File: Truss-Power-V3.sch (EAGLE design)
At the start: 31 parts, among them J1 XF2L-0535-1, U1 TPS61090, U2 MCP73831T-2ACI/OT, U3 MAX17044, X1 22-23-2021, X2 MicroB, X3 22-23-2021, X4 CON-1PIN

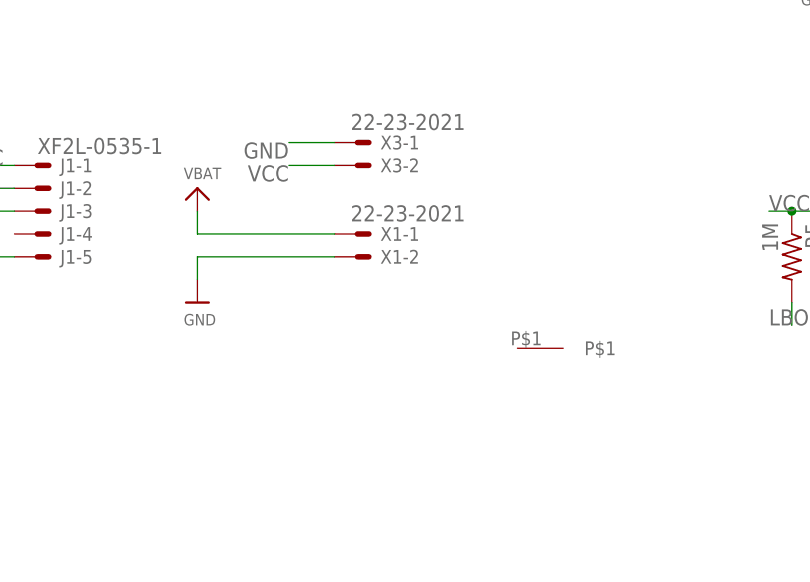
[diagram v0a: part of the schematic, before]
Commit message: v3 truss power battery connector updated
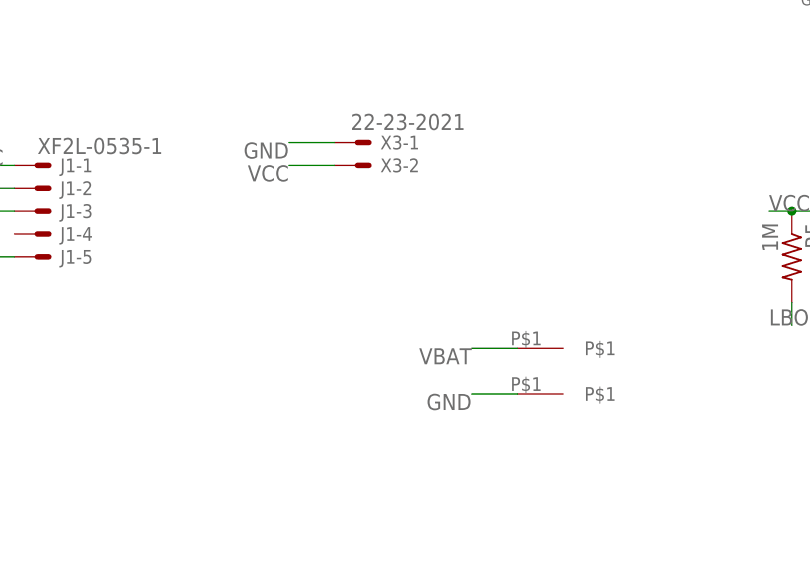
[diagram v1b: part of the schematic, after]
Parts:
- removed X1: 22-23-2021, con-molex:22-23-2021
- added X5: CON-1PIN, NewPart:CON-1PIN
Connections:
- net GND: now also X5.P$1; no longer X1-2.S
- net VBAT: now also X4.P$1; no longer X1-1.S
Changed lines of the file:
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@@
 <?xml version="1.0" encoding="utf-8"?>
 <!DOCTYPE eagle SYSTEM "eagle.dtd">
-<eagle version="8.3.2">
+<eagle version="8.4.3">
 <drawing>
 <settings>
@@
 <part name="C3" library="microbuilder" deviceset="CAP_CERAMIC" device="0805-NOOUTLINE" value="10µF"/>
 <part name="U$15" library="microbuilder" deviceset="GND" device=""/>
-<part name="X1" library="con-molex" library_urn="urn:adsk.eagle:library:165" deviceset="22-23-2021" device=""/>
-<part name="U$16" library="microbuilder" deviceset="VBAT" device=""/>
-<part name="U$17" library="microbuilder" deviceset="GND" device=""/>
 <part name="U3" library="NewPart" deviceset="MAX17044" device=""/>
 <part name="R6" library="resistor" deviceset="R-US_" device="R0402" value="1K"/>
@@
 <part name="R7" library="resistor" deviceset="R-US_" device="R0402" value="470"/>
 <part name="X4" library="NewPart" deviceset="CON-1PIN" device=""/>
+<part name="X5" library="NewPart" deviceset="CON-1PIN" device=""/>
 </parts>
 <sheets>
@@
 <instance part="C3" gate="G$1" x="119.38" y="76.2"/>
 <instance part="U$15" gate="G$1" x="119.38" y="68.58"/>
-<instance part="X1" gate="-1" x="99.06" y="15.24"/>
-<instance part="X1" gate="-2" x="99.06" y="12.7"/>
-<instance part="U$16" gate="G$1" x="81.28" y="20.32"/>
-<instance part="U$17" gate="G$1" x="81.28" y="7.62"/>
 <instance part="U3" gate="G$1" x="175.26" y="63.5"/>
 <instance part="R6" gate="G$1" x="142.24" y="68.58"/>
@@
 <instance part="R7" gate="G$1" x="60.96" y="76.2" rot="R180"/>
 <instance part="X4" gate="G$1" x="121.92" y="2.54"/>
+<instance part="X5" gate="G$1" x="121.92" y="-2.54"/>
 </instances>
 <busses>
@@
 </segment>
 <segment>
-<pinref part="X1" gate="-2" pin="S"/>
-<pinref part="U$17" gate="G$1" pin="GND"/>
-<wire x1="96.52" y1="12.7" x2="81.28" y2="12.7" width="0.1524" layer="91"/>
-<wire x1="81.28" y1="12.7" x2="81.28" y2="10.16" width="0.1524" layer="91"/>
-</segment>
-<segment>
 <wire x1="157.48" y1="53.34" x2="157.48" y2="45.72" width="0.1524" layer="91"/>
 <pinref part="U3" gate="G$1" pin="GND"/>
@@
 <wire x1="48.26" y1="43.18" x2="55.88" y2="43.18" width="0.1524" layer="91"/>
 <wire x1="55.88" y1="43.18" x2="55.88" y2="40.64" width="0.1524" layer="91"/>
+</segment>
+<segment>
+<pinref part="X5" gate="G$1" pin="P$1"/>
+<wire x1="116.84" y1="-2.54" x2="111.76" y2="-2.54" width="0.1524" layer="91"/>
+<label x="111.76" y="-2.54" size="1.778" layer="95" rot="R180"/>
 </segment>
 </net>
@@
 </segment>
 <segment>
-<pinref part="U$16" gate="G$1" pin="VBAT"/>
-<pinref part="X1" gate="-1" pin="S"/>
-<wire x1="81.28" y1="17.78" x2="81.28" y2="15.24" width="0.1524" layer="91"/>
-<wire x1="81.28" y1="15.24" x2="96.52" y2="15.24" width="0.1524" layer="91"/>
-</segment>
-<segment>
 <pinref part="U$8" gate="G$1" pin="VBAT"/>
 <pinref part="R11" gate="G$1" pin="1"/>
@@
 <label x="50.8" y="20.32" size="1.778" layer="95"/>
 </segment>
+<segment>
+<pinref part="X4" gate="G$1" pin="P$1"/>
+<wire x1="116.84" y1="2.54" x2="111.76" y2="2.54" width="0.1524" layer="91"/>
+<label x="111.76" y="2.54" size="1.778" layer="95" rot="R180"/>
+</segment>
 </net>

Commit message: 6-Pin FPC updated.
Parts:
- added D1: (no value), diode:DIODE-SOD523
- added IC1: 74AUC1G06DCK, 74xx-little-us:74AUC1G06DCK
- J1: value XF2L-0535-1 -> XF2L-0625-1; device con-omron:XF2L-0535-1 -> con-omron:XF2L-0625-1
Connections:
- removed net EN_SIG: J1-5.MS
- removed net EN_SW: J1-3.MS
- new net DETSW_P: J1-4.MS
- new net PWRSW_P: D1.A, J1-3.MS
- net LEDSOC: now also J1-1.MS; no longer J1-1.MSV
- net SCL: now also J1-6.MS
- net SDA: now also J1-5.MS
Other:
- note added: "BOOST"
- note added: "CHARGER"
- note added: "CONNECTOR"
- note added: "GAUGE"

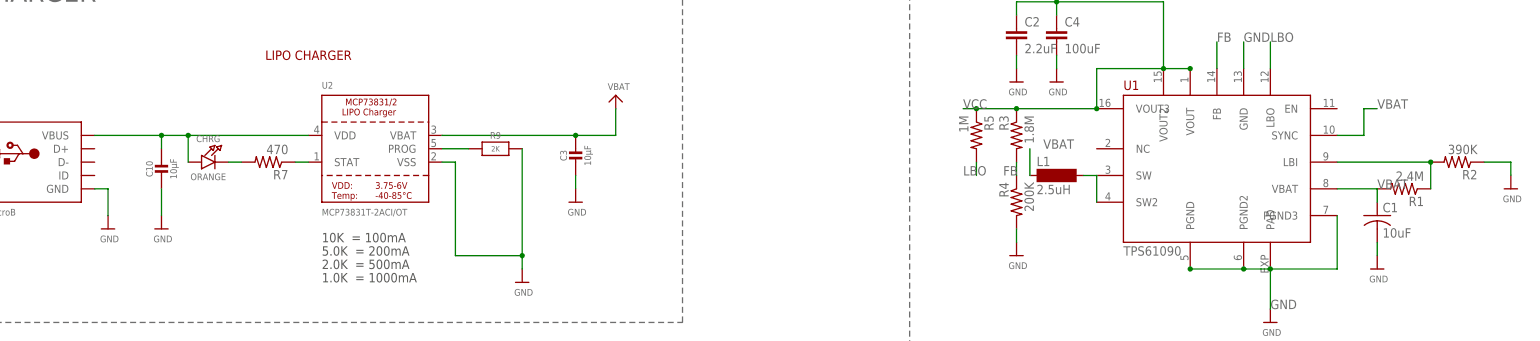
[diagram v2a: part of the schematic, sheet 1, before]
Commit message: Charger circuitry updated; Inverter and diode-or added for Boost EN
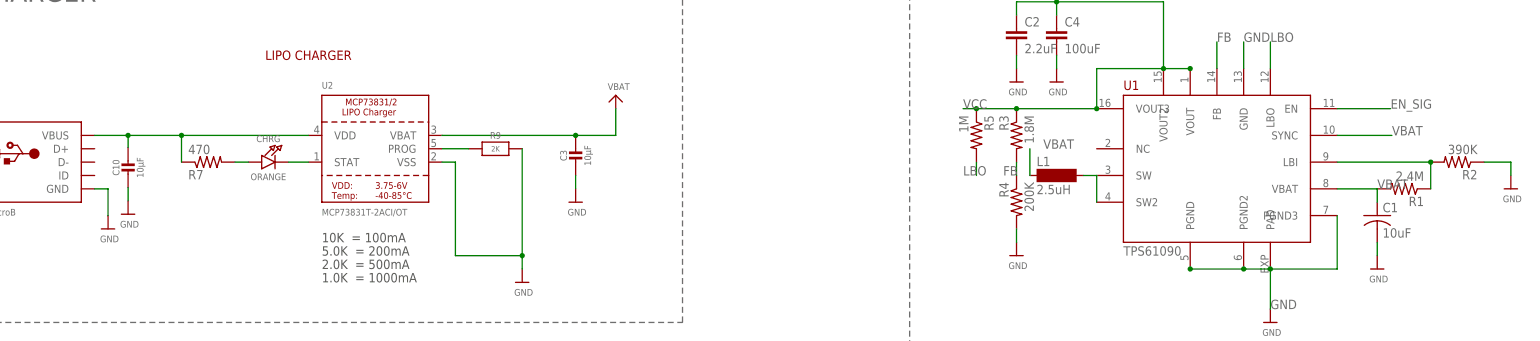
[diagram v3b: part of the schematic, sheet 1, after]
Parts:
- removed IC1: 74AUC1G06DCK, 74xx-little-us:74AUC1G06DCK
- added D2: (no value), diode:DIODE-SOD523
- added U$16: INVERTER-GATE, NewPart:INVERTER-GATE
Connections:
- removed net N$12: CHRG.C, R7.2
- removed net N$13: R7.1, U2.STAT
- new net EN_SIG: D1.C, D2.C, U1.EN
- new net N$5: D2.A, U$16.P$2
- new net N$6: CHRG.A, R7.2
- new net N$7: CHRG.C, U2.STAT
- net DETSW_P: now also U$16.P$1
- net GND: now also U$16.GND
- net VBAT: now also U$16.VBAT
- net VBUS: now also R7.1; no longer CHRG.A
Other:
- moved on the sheet: C10, CHRG, R7

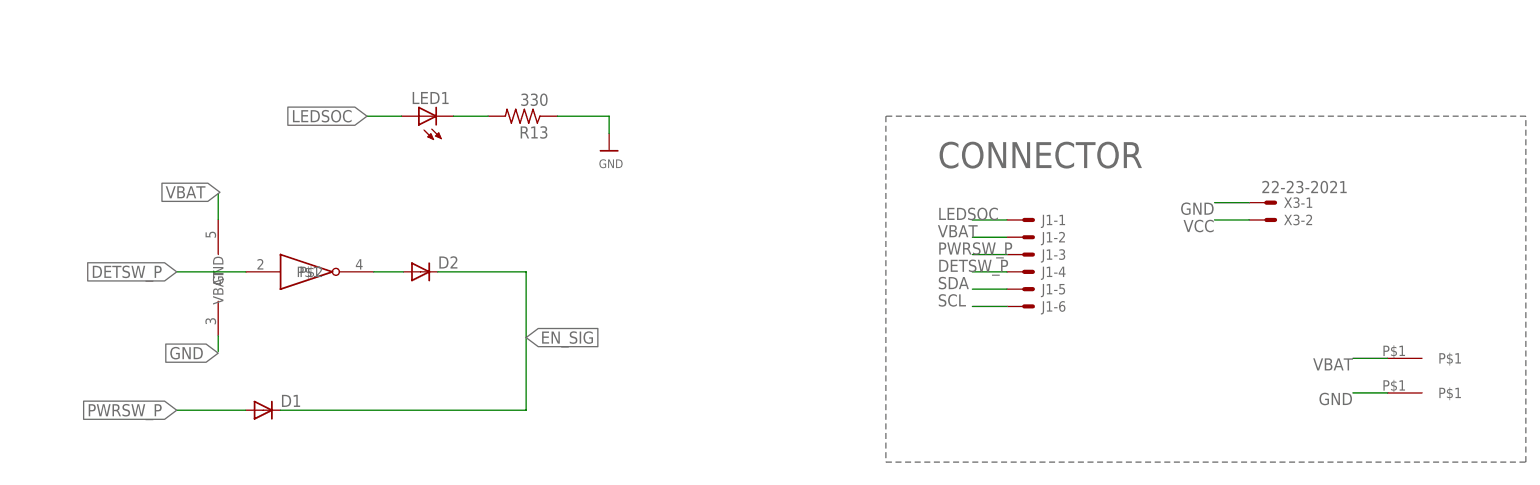
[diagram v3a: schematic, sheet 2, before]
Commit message: XOR Gate added in library; XOR gate added for Boost EN
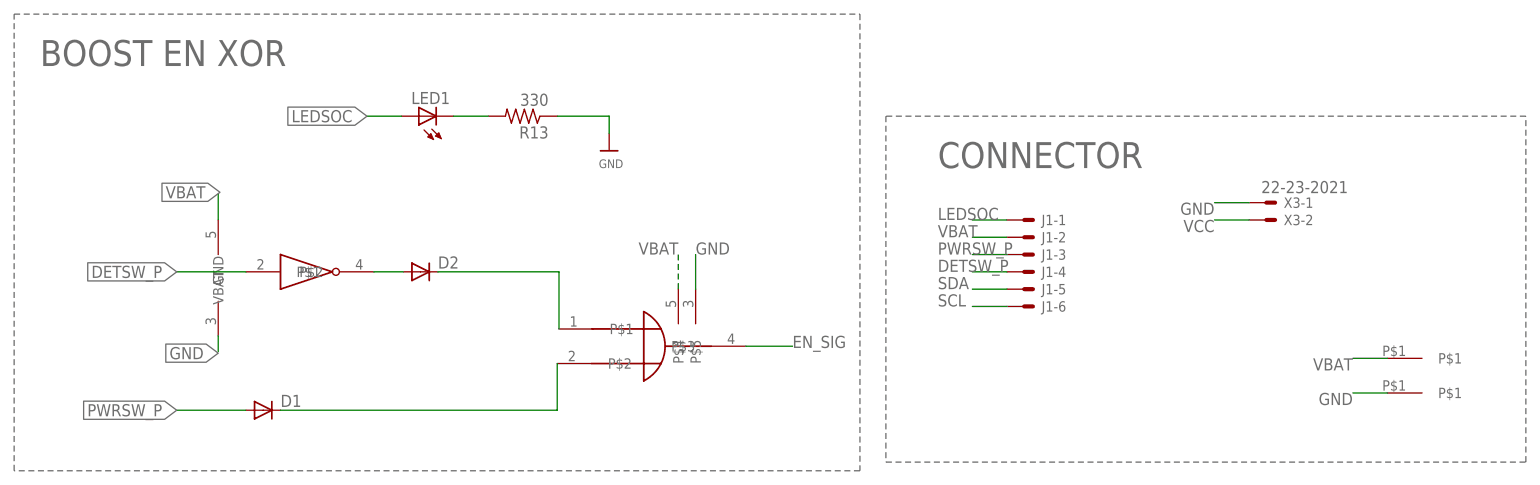
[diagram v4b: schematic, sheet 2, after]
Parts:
- added U4: SN74LVC1G86DC1LR, NewPart:SN74LVC1G86DC1LR
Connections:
- new net DETSW_D: D2.C, U4.P$1
- new net PWRSW_D: D1.C, U4.P$2
- net EN_SIG: now also U4.P$3; no longer D1.C, D2.C
- net GND: now also U4.P$5
- net VBAT: now also U4.P$4
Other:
- note added: "BOOST EN XOR"
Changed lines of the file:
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@@
 <part name="U$16" library="NewPart" deviceset="INVERTER-GATE" device=""/>
 <part name="D2" library="diode" library_urn="urn:adsk.eagle:library:210" deviceset="DIODE-" device="SOD523" package3d_urn="urn:adsk.eagle:package:43410/1"/>
+<part name="U4" library="NewPart" deviceset="SN74LVC1G86DC1LR" device=""/>
 </parts>
 <sheets>
@@
 <wire x1="200.66" y1="76.2" x2="106.68" y2="76.2" width="0.1524" layer="95" style="longdash"/>
 <text x="114.3" y="68.58" size="3.81" layer="95">CONNECTOR</text>
+<wire x1="-21.336" y1="91.186" x2="102.87" y2="91.186" width="0.1524" layer="95" style="longdash"/>
+<wire x1="102.87" y1="91.186" x2="102.87" y2="24.13" width="0.1524" layer="95" style="longdash"/>
+<wire x1="102.87" y1="24.13" x2="-21.336" y2="24.13" width="0.1524" layer="95" style="longdash"/>
+<wire x1="-21.336" y1="24.13" x2="-21.336" y2="91.186" width="0.1524" layer="95" style="longdash"/>
+<text x="-17.526" y="83.566" size="3.81" layer="95">BOOST EN XOR</text>
 </plain>
 <instances>
@@
 <instance part="U$16" gate="G$1" x="20.32" y="53.34"/>
 <instance part="D2" gate="G$1" x="38.354" y="53.34"/>
+<instance part="U4" gate="G$1" x="71.12" y="42.418"/>
 </instances>
 <busses>
@@
 <label x="8.636" y="41.402" size="1.778" layer="95" rot="R180" xref="yes"/>
 </segment>
+<segment>
+<wire x1="78.74" y1="55.88" x2="78.74" y2="50.8" width="0.1524" layer="91"/>
+<pinref part="U4" gate="G$1" pin="P$5"/>
+<label x="78.74" y="55.88" size="1.778" layer="95"/>
+</segment>
 </net>
 <net name="VBAT" class="0">
@@
 <label x="8.89" y="65.024" size="1.778" layer="95" rot="R180" xref="yes"/>
 </segment>
+<segment>
+<pinref part="U4" gate="G$1" pin="P$4"/>
+<wire x1="76.2" y1="50.8" x2="76.2" y2="55.88" width="0.1524" layer="91" style="longdash"/>
+<label x="76.2" y="57.658" size="1.778" layer="95" rot="R180"/>
+</segment>
 </net>
 <net name="VCC" class="0">
@@
 </segment>
 </net>
+<net name="DETSW_D" class="0">
+<segment>
+<pinref part="D2" gate="G$1" pin="C"/>
+<wire x1="40.894" y1="53.34" x2="58.674" y2="53.34" width="0.1524" layer="91"/>
+<pinref part="U4" gate="G$1" pin="P$1"/>
+<wire x1="58.674" y1="44.958" x2="58.674" y2="53.34" width="0.1524" layer="91"/>
+</segment>
+</net>
+<net name="PWRSW_D" class="0">
+<segment>
+<pinref part="D1" gate="G$1" pin="C"/>
+<wire x1="17.78" y1="33.02" x2="58.42" y2="33.02" width="0.1524" layer="91"/>
+<pinref part="U4" gate="G$1" pin="P$2"/>
+<wire x1="58.42" y1="39.878" x2="58.42" y2="33.02" width="0.1524" layer="91"/>
+</segment>
+</net>
 <net name="EN_SIG" class="0">
 <segment>
-<pinref part="D1" gate="G$1" pin="C"/>
-<wire x1="17.78" y1="33.02" x2="53.848" y2="33.02" width="0.1524" layer="91"/>
-<pinref part="D2" gate="G$1" pin="C"/>
-<wire x1="40.894" y1="53.34" x2="53.848" y2="53.34" width="0.1524" layer="91"/>
-<wire x1="53.848" y1="53.34" x2="53.848" y2="33.02" width="0.1524" layer="91"/>
-<label x="53.848" y="43.688" size="1.778" layer="95" xref="yes"/>
-</segment>
-</net>
+<pinref part="U4" gate="G$1" pin="P$3"/>
+<wire x1="86.106" y1="42.418" x2="92.964" y2="42.418" width="0.1524" layer="91"/>
+<label x="92.964" y="42.164" size="1.778" layer="95"/>
+</segment>
+</net>

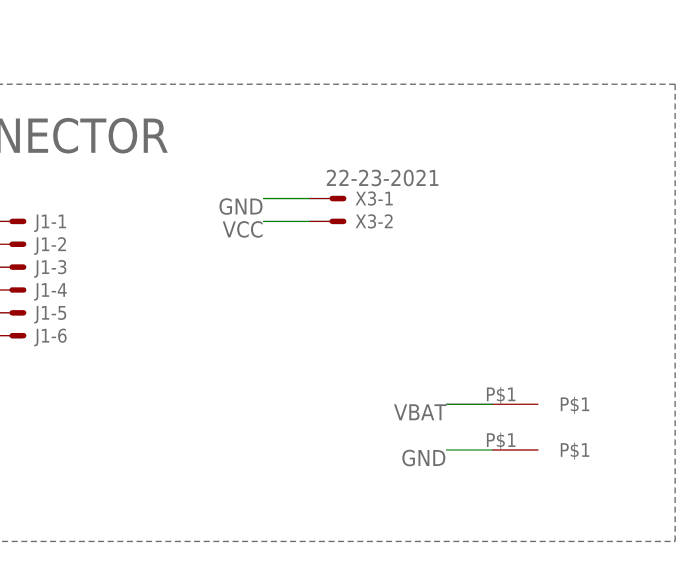
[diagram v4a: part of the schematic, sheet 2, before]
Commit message: To add signal control
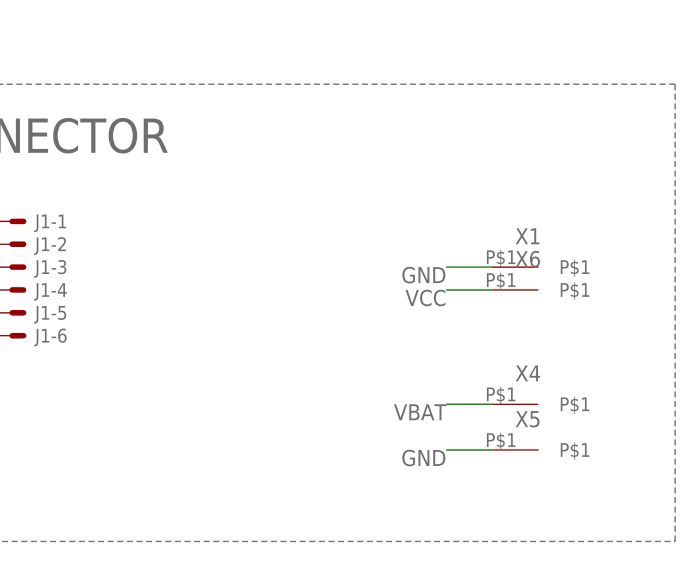
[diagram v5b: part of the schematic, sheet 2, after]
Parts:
- removed X3: 22-23-2021, con-molex:22-23-2021
- added X1, X6: CON-1PIN, NewPart:CON-1PIN
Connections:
- net GND: now also X1.P$1; no longer X3-1.S
- net VCC: now also X6.P$1; no longer X3-2.S
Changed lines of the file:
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@@
 <setting verticaltext="up"/>
 </settings>
-<grid distance="0.01" unitdist="inch" unit="inch" style="lines" multiple="1" display="yes" altdistance="0.01" altunitdist="inch" altunit="inch"/>
+<grid distance="0.1" unitdist="inch" unit="inch" style="lines" multiple="1" display="no" altdistance="0.01" altunitdist="inch" altunit="inch"/>
 <layers>
 <layer number="1" name="Top" color="4" fill="1" visible="no" active="no"/>
@@
 <part name="U$8" library="microbuilder" deviceset="VBAT" device=""/>
 <part name="U1" library="NewPart" deviceset="TPS61090" device=""/>
-<part name="X3" library="con-molex" deviceset="22-23-2021" device=""/>
 <part name="R1" library="adafruit" deviceset="R-US_" device="R0603" value="2.4M"/>
 <part name="R2" library="adafruit" deviceset="R-US_" device="R0603" value="390K"/>
@@
 <part name="D2" library="diode" library_urn="urn:adsk.eagle:library:210" deviceset="DIODE-" device="SOD523" package3d_urn="urn:adsk.eagle:package:43410/1"/>
 <part name="U4" library="NewPart" deviceset="SN74LVC1G86DC1LR" device=""/>
+<part name="X1" library="NewPart" deviceset="CON-1PIN" device=""/>
+<part name="X6" library="NewPart" deviceset="CON-1PIN" device=""/>
 </parts>
 <sheets>
@@
 </plain>
 <instances>
-<instance part="X3" gate="-1" x="162.56" y="63.5"/>
-<instance part="X3" gate="-2" x="162.56" y="60.96"/>
 <instance part="LED1" gate="G$1" x="38.1" y="76.2" rot="R90"/>
 <instance part="R13" gate="G$1" x="53.34" y="76.2" rot="R180"/>
@@
 <instance part="D2" gate="G$1" x="38.354" y="53.34"/>
 <instance part="U4" gate="G$1" x="71.12" y="42.418"/>
+<instance part="X1" gate="G$1" x="185.42" y="55.88"/>
+<instance part="X6" gate="G$1" x="185.42" y="53.34"/>
 </instances>
 <busses>
@@
 <net name="GND" class="0">
 <segment>
-<wire x1="160.02" y1="63.5" x2="154.94" y2="63.5" width="0.1524" layer="91"/>
-<label x="154.94" y="63.5" size="1.778" layer="95" rot="R180"/>
-<pinref part="X3" gate="-1" pin="S"/>
-</segment>
-<segment>
 <pinref part="R13" gate="G$1" pin="1"/>
 <pinref part="U$22" gate="G$1" pin="GND"/>
@@
 <label x="78.74" y="55.88" size="1.778" layer="95"/>
 </segment>
+<segment>
+<pinref part="X1" gate="G$1" pin="P$1"/>
+<wire x1="180.34" y1="55.88" x2="175.26" y2="55.88" width="0.1524" layer="91"/>
+<label x="175.26" y="55.88" size="1.778" layer="95" rot="R180"/>
+</segment>
 </net>
 <net name="VBAT" class="0">
@@
 <net name="VCC" class="0">
 <segment>
-<wire x1="160.02" y1="60.96" x2="154.94" y2="60.96" width="0.1524" layer="91"/>
-<label x="154.94" y="60.96" size="1.778" layer="95" rot="R180"/>
-<pinref part="X3" gate="-2" pin="S"/>
-</segment>
-</net>
+<pinref part="X6" gate="G$1" pin="P$1"/>
+<wire x1="180.34" y1="53.34" x2="175.26" y2="53.34" width="0.1524" layer="91"/>
+<label x="175.26" y="53.34" size="1.778" layer="95" rot="R180"/>
+</segment>
+</net>
